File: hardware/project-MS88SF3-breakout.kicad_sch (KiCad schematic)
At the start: 27 parts, among them J1 Conn_02x05_Odd_Even, J2 S2B-PH-SM4-TB(LF)(SN), J3 USB4105-GF-A, J4 Conn_01x12_Pin, J5 Conn_01x16_Pin, U1 MS88SF3_NRF52840

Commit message: Fix ERC error
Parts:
- S1: footprint 435151014824 -> 435151014824:435151014824
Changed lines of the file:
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@@
 			)
 		)
-		(property "Footprint" "435151014824"
+		(property "Footprint" "435151014824:435151014824"
 			(at 82.55 167.64 0)
 			(effects
@@
 			)
 		)
-		(property "Description" ""
+		(property "Description" "435151014824"
 			(at 64.77 167.64 0)
 			(effects

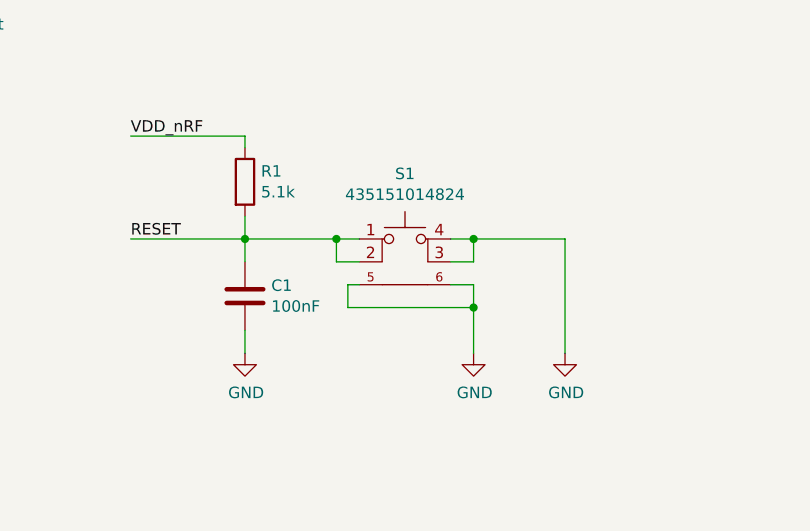
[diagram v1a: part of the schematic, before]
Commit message: Change reset button
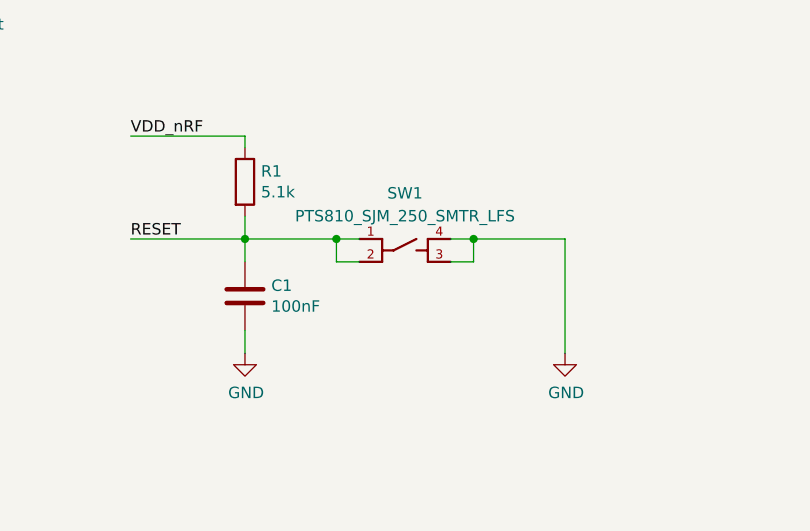
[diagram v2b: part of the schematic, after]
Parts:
- removed S1: 435151014824, 435151014824:435151014824, symbol 435151014824:435151014824
- added SW1: PTS810_SJM_250_SMTR_LFS, PTS810-SJM-250-SMTR-LFS:SW_PTS810_SJM_250_SMTR_LFS, symbol PTS810_SJM_250_SMTR_LFS:PTS810_SJM_250_SMTR_LFS
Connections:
- net GND: now also SW1.3, SW1.4
- net RESET: now also SW1.1, SW1.2
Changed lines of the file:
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@@
 	)
 	(junction
-		(at 72.39 175.26)
-		(diameter 0)
-		(color 0 0 0 0)
-	)
-	(junction
 		(at 229.87 34.29)
 		(diameter 0)
@@
 	(wire
 		(pts
-			(xy 72.39 175.26) (xy 72.39 180.34)
-		)
-		(stroke
-			(width 0)
-			(type default)
-		)
-	)
-	(wire
-		(pts
 			(xy 46.99 165.1) (xy 46.99 167.64)
 		)
@@
 	(wire
 		(pts
-			(xy 72.39 172.72) (xy 72.39 175.26)
-		)
-		(stroke
-			(width 0)
-			(type default)
-		)
-	)
-	(wire
-		(pts
 			(xy 128.27 52.07) (xy 137.16 52.07)
 		)
@@
 	(wire
 		(pts
-			(xy 59.69 172.72) (xy 58.42 172.72)
-		)
-		(stroke
-			(width 0)
-			(type default)
-		)
-	)
-	(wire
-		(pts
 			(xy 100.33 116.84) (xy 91.44 116.84)
 		)
@@
 	(wire
 		(pts
-			(xy 58.42 172.72) (xy 58.42 175.26)
-		)
-		(stroke
-			(width 0)
-			(type default)
-		)
-	)
-	(wire
-		(pts
 			(xy 251.46 125.73) (xy 254 125.73)
 		)
@@
 	(wire
 		(pts
-			(xy 69.85 172.72) (xy 72.39 172.72)
-		)
-		(stroke
-			(width 0)
-			(type default)
-		)
-	)
-	(wire
-		(pts
 			(xy 21.59 63.5) (xy 30.48 63.5)
 		)
@@
 	(wire
 		(pts
-			(xy 58.42 175.26) (xy 72.39 175.26)
-		)
-		(stroke
-			(width 0)
-			(type default)
-		)
-	)
-	(wire
-		(pts
 			(xy 213.36 39.37) (xy 217.17 39.37)
 		)
@@
 	)
 	(symbol
-		(lib_id "435151014824:435151014824")
-		(at 64.77 167.64 0)
-		(unit 1)
-		(exclude_from_sim no)
-		(in_bom yes)
-		(on_board yes)
-		(dnp no)
-		(property "Reference" "S1"
-			(at 64.77 160.401 0)
-			(effects
-				(font
-					(size 1.27 1.27)
-				)
-			)
-		)
-		(property "Value" "435151014824"
-			(at 64.77 162.7124 0)
-			(effects
-				(font
-					(size 1.27 1.27)
-				)
-			)
-		)
-		(property "Footprint" "435151014824:435151014824"
-			(at 82.55 167.64 0)
-			(effects
-				(font
-					(size 1.27 1.27)
-				)
-				(justify left bottom)
-				(hide yes)
-			)
-		)
-		(property "Datasheet" ""
-			(at 64.77 165.1 0)
-			(effects
-				(font
-					(size 1.27 1.27)
-				)
-				(justify left bottom)
-				(hide yes)
-			)
-		)
-		(property "Description" "435151014824"
-			(at 64.77 167.64 0)
-			(effects
-				(font
-					(size 1.27 1.27)
-				)
-				(hide yes)
-			)
-		)
-		(property "PART-NUMBER" "435151014824"
-			(at 82.55 165.1 0)
-			(effects
-				(font
-					(size 1.27 1.27)
-				)
-				(justify left bottom)
-				(hide yes)
-			)
-		)
-		(property "QTY" "9500"
-			(at 74.93 167.64 0)
-			(effects
-				(font
-					(size 1.27 1.27)
-				)
-				(justify left bottom)
-				(hide yes)
-			)
-		)
-		(property "DATASHEET-URL" "https://www.we-online.com/catalog/datasheet/435151014824 .pdf"
-			(at 74.93 170.18 0)
-			(effects
-				(font
-					(size 1.27 1.27)
-				)
-				(justify left bottom)
-				(hide yes)
-			)
-		)
-		(property "H" "1.4mm"
-			(at 74.93 165.1 0)
-			(effects
-				(font
-					(size 1.27 1.27)
-				)
-				(justify left bottom)
-				(hide yes)
-			)
-		)
-		(property "OPERATION-FORCE" "240g"
-			(at 74.93 162.56 0)
-			(effects
-				(font
-					(size 1.27 1.27)
-				)
-				(justify left bottom)
-				(hide yes)
-			)
-		)
-		(property "VALUE" "435151014824"
-			(at 82.55 162.56 0)
-			(effects
-				(font
-					(size 1.27 1.27)
-				)
-				(justify left bottom)
-				(hide yes)
-			)
-		)
-		(pin "5"
-		)
-		(pin "1"
-		)
-		(pin "4"
-		)
-		(pin "3"
-		)
-		(pin "6"
-		)
-		(pin "2"
-		)
-		(instances
-			(project "project-MS88SF3-breakout"
-				(path "/3e0804a6-abc2-4b5d-ae97-2c771c876220"
-					(reference "S1")
-					(unit 1)
-				)
-			)
-		)
-	)
-	(symbol
-		(lib_id "power:GND")
-		(at 72.39 180.34 0)
-		(unit 1)
-		(exclude_from_sim no)
-		(in_bom yes)
-		(on_board yes)
-		(dnp no)
-		(property "Reference" "#PWR03"
-			(at 72.39 186.69 0)
-			(effects
-				(font
-					(size 1.27 1.27)
-				)
-				(hide yes)
-			)
-		)
-		(property "Value" "GND"
-			(at 72.517 184.7342 0)
-			(effects
-				(font
-					(size 1.27 1.27)
-				)
-			)
-		)
-		(property "Footprint" ""
-			(at 72.39 180.34 0)
-			(effects
-				(font
-					(size 1.27 1.27)
-				)
-				(hide yes)
-			)
-		)
-		(property "Datasheet" ""
-			(at 72.39 180.34 0)
-			(effects
-				(font
-					(size 1.27 1.27)
-				)
-				(hide yes)
-			)
-		)
-		(property "Description" ""
-			(at 72.39 180.34 0)
-			(effects
-				(font
-					(size 1.27 1.27)
-				)
-				(hide yes)
-			)
-		)
-		(pin "1"
-		)
-		(instances
-			(project "project-MS88SF3-breakout"
-				(path "/3e0804a6-abc2-4b5d-ae97-2c771c876220"
-					(reference "#PWR03")
-					(unit 1)
-				)
-			)
-		)
-	)
-	(symbol
 		(lib_id "MS88SF3_NRF52840:MS88SF3_NRF52840")
 		(at 60.96 76.2 0)
@@
 					(unit 1)
 				)
+			)
+		)
+	)
+	(symbol
+		(lib_id "PTS810_SJM_250_SMTR_LFS:PTS810_SJM_250_SMTR_LFS")
+		(at 64.77 167.64 0)
+		(unit 1)
+		(exclude_from_sim no)
+		(in_bom yes)
+		(on_board yes)
+		(dnp no)
+		(fields_autoplaced yes)
+		(property "Reference" "SW1"
+			(at 64.77 162.56 0)
+			(effects
+				(font
+					(size 1.27 1.27)
+				)
+			)
+		)
+		(property "Value" "PTS810_SJM_250_SMTR_LFS"
+			(at 64.77 165.1 0)
+			(effects
+				(font
+					(size 1.27 1.27)
+				)
+			)
+		)
+		(property "Footprint" "PTS810-SJM-250-SMTR-LFS:SW_PTS810_SJM_250_SMTR_LFS"
+			(at 64.77 167.64 0)
+			(effects
+				(font
+					(size 1.27 1.27)
+				)
+				(justify bottom)
+				(hide yes)
+			)
+		)
+		(property "Datasheet" ""
+			(at 64.77 167.64 0)
+			(effects
+				(font
+					(size 1.27 1.27)
+				)
+				(hide yes)
+			)
+		)
+		(property "Description" ""
+			(at 64.77 167.64 0)
+			(effects
+				(font
+					(size 1.27 1.27)
+				)
+				(hide yes)
+			)
+		)
+		(property "DigiKey_Part_Number" "CKN10502TR-ND"
+			(at 64.77 167.64 0)
+			(effects
+				(font
+					(size 1.27 1.27)
+				)
+				(justify bottom)
+				(hide yes)
+			)
+		)
+		(property "SnapEDA_Link" "https://www.snapeda.com/parts/PTS810%20SJM%20250%20SMTR%20LFS/C%2526K/view-part/?ref=snap"
+			(at 64.77 167.64 0)
+			(effects
+				(font
+					(size 1.27 1.27)
+				)
+				(justify bottom)
+				(hide yes)
+			)
+		)
+		(property "Description_1" "\nTactile Switch SPST-NO Top Actuated Surface Mount\n"
+			(at 64.77 167.64 0)
+			(effects
+				(font
+					(size 1.27 1.27)
+				)
+				(justify bottom)
+				(hide yes)
+			)
+		)
+		(property "Package" "None"
+			(at 64.77 167.64 0)
+			(effects
+				(font
+					(size 1.27 1.27)
+				)
+				(justify bottom)
+				(hide yes)
+			)
+		)
+		(property "Check_prices" "https://www.snapeda.com/parts/PTS810%20SJM%20250%20SMTR%20LFS/C%2526K/view-part/?ref=eda"
+			(at 64.77 167.64 0)
+			(effects
+				(font
+					(size 1.27 1.27)
+				)
+				(justify bottom)
+				(hide yes)
+			)
+		)
+		(property "STANDARD" "Manufacturer Recommendations"
+			(at 64.77 167.64 0)
+			(effects
+				(font
+					(size 1.27 1.27)
+				)
+				(justify bottom)
+				(hide yes)
+			)
+		)
+		(property "MF" "C&K"
+			(at 64.77 167.64 0)
+			(effects
+				(font
+					(size 1.27 1.27)
+				)
+				(justify bottom)
+				(hide yes)
+			)
+		)
+		(property "MP" "PTS810 SJM 250 SMTR LFS"
+			(at 64.77 167.64 0)
+			(effects
+				(font
+					(size 1.27 1.27)
+				)
+				(justify bottom)
+				(hide yes)
+			)
+		)
+		(property "MANUFACTURER" "CnK"
+			(at 64.77 167.64 0)
+			(effects
+				(font
+					(size 1.27 1.27)
+				)
+				(justify bottom)
+				(hide yes)
+			)
+		)
+		(pin "4"
+		)
+		(pin "3"
+		)
+		(pin "2"
+		)
+		(pin "1"
+		)
+		(instances
+			(project "project-MS88SF3-breakout"
+				(path "/3e0804a6-abc2-4b5d-ae97-2c771c876220"
+					(reference "SW1")
+					(unit 1)
+				)

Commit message: User SolderJumper-2 footprint without center soldermask
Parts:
- JP1: footprint Jumper:SolderJumper-2_P1.3mm_Bridged_RoundedPad1.0x1.5mm -> mine:SolderJumper-2_P1.3mm_Bridged_RoundedPad1.0x1.5mm
- JP2: footprint Jumper:SolderJumper-2_P1.3mm_Open_RoundedPad1.0x1.5mm -> mine:SolderJumper-2_P1.3mm_Open_RoundedPad1.0x1.5mm
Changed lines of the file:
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@@
 			)
 		)
-		(property "Footprint" "Jumper:SolderJumper-2_P1.3mm_Bridged_RoundedPad1.0x1.5mm"
+		(property "Footprint" "mine:SolderJumper-2_P1.3mm_Bridged_RoundedPad1.0x1.5mm"
 			(at 236.22 39.37 0)
 			(effects
@@
 			)
 		)
-		(property "Footprint" "Jumper:SolderJumper-2_P1.3mm_Open_RoundedPad1.0x1.5mm"
+		(property "Footprint" "mine:SolderJumper-2_P1.3mm_Open_RoundedPad1.0x1.5mm"
 			(at 242.57 30.48 0)
 			(effects

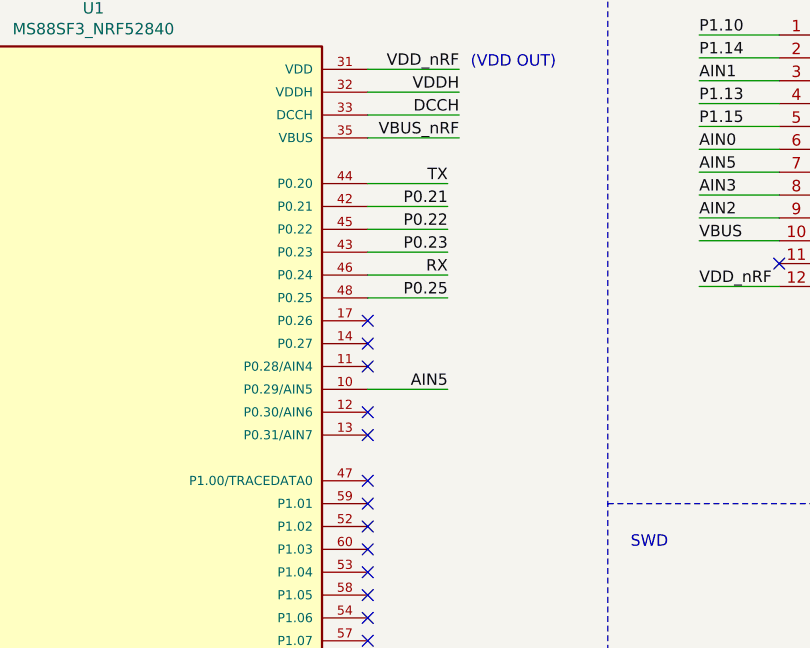
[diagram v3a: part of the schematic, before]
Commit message: Move TX to SWO
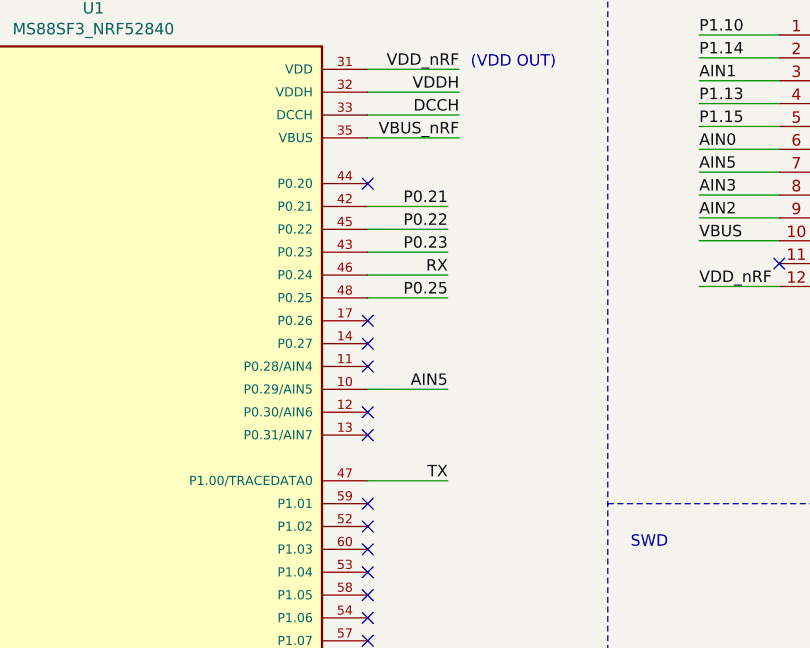
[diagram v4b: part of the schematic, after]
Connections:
- net TX: now also U1.47 (P1.00/TRACEDATA0); no longer U1.44 (P0.20)
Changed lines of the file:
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@@
 	)
 	(no_connect
-		(at 91.44 78.74)
+		(at 91.44 45.72)
 	)
 	(no_connect
@@
 	(wire
 		(pts
-			(xy 100.33 45.72) (xy 91.44 45.72)
+			(xy 100.33 78.74) (xy 91.44 78.74)
 		)
 		(stroke
@@
 	)
 	(label "TX"
-		(at 100.33 45.72 180)
-		(fields_autoplaced yes)
-		(effects
+		(at 100.33 78.74 180)
+		(fields_autoplaced yes)
+		(effects

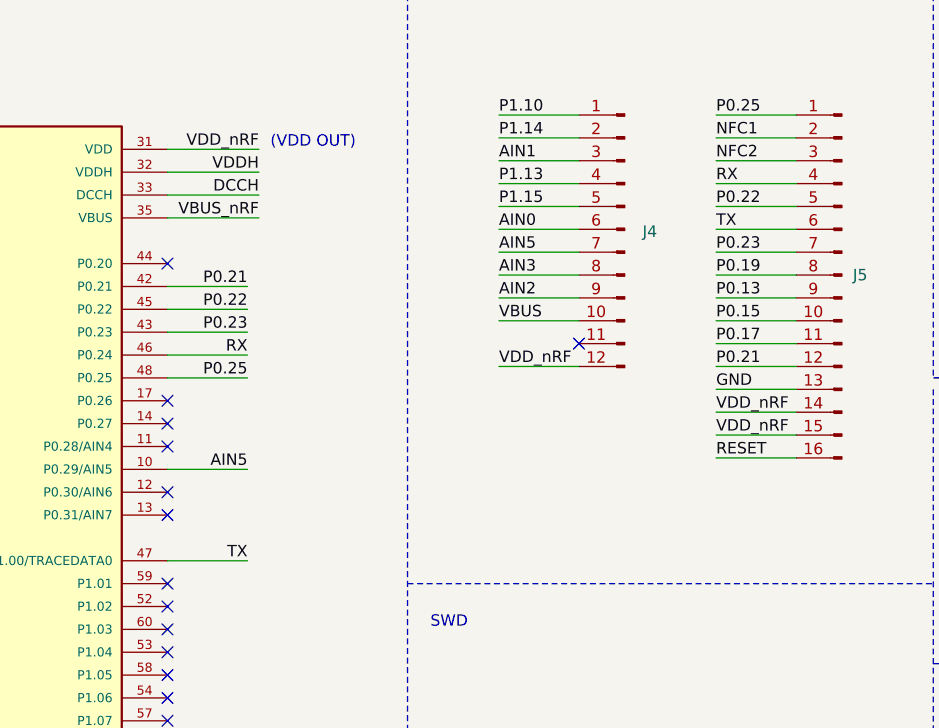
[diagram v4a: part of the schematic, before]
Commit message: Change header RX/TX to gpios
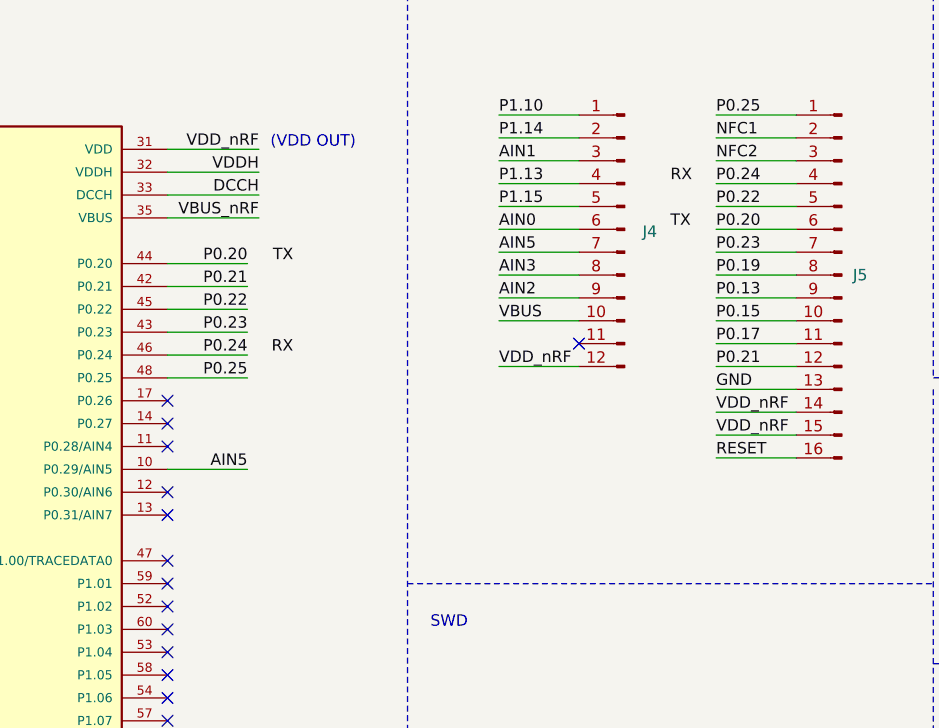
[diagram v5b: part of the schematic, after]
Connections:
- net RX: no longer J5.4 (Pin_4), U1.46 (P0.24)
- net TX: no longer J5.6 (Pin_6), U1.47 (P1.00/TRACEDATA0)
- net P0.20: now reaches U1.44 (P0.20)
- net P0.20: now also J5.6 (Pin_6)
- new net P0.24: J5.4 (Pin_4), U1.46 (P0.24)
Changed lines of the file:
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@@
 	)
 	(no_connect
-		(at 91.44 45.72)
+		(at 91.44 78.74)
 	)
 	(no_connect
@@
 	(wire
 		(pts
-			(xy 100.33 78.74) (xy 91.44 78.74)
+			(xy 100.33 45.72) (xy 91.44 45.72)
 		)
 		(stroke
@@
 		)
 	)
+	(label "P0.24"
+		(at 152.4 36.83 0)
+		(fields_autoplaced yes)
+		(effects
+			(font
+				(size 1.27 1.27)
+			)
+			(justify left bottom)
+		)
+	)
+	(label "P0.24"
+		(at 100.33 55.88 180)
+		(fields_autoplaced yes)
+		(effects
+			(font
+				(size 1.27 1.27)
+			)
+			(justify right bottom)
+		)
+	)
 	(label "P0.21"
 		(at 152.4 57.15 0)
@@
 	)
 	(label "TX"
-		(at 152.4 41.91 0)
+		(at 147.32 41.91 0)
 		(fields_autoplaced yes)
 		(effects
@@
 	)
 	(label "TX"
-		(at 100.33 78.74 180)
+		(at 105.41 45.72 180)
 		(fields_autoplaced yes)
 		(effects
@@
 	)
 	(label "RX"
-		(at 100.33 55.88 180)
+		(at 105.41 55.88 180)
 		(fields_autoplaced yes)
 		(effects
@@
 	)
 	(label "RX"
-		(at 152.4 36.83 0)
+		(at 147.32 36.83 0)
 		(fields_autoplaced yes)
 		(effects
@@
 		)
 	)
+	(label "P0.20"
+		(at 100.33 45.72 180)
+		(fields_autoplaced yes)
+		(effects
+			(font
+				(size 1.27 1.27)
+			)
+			(justify right bottom)
+		)
+	)
 	(label "D+"
 		(at 186.69 146.05 0)
@@
 		)
 	)
+	(label "P0.20"
+		(at 152.4 41.91 0)
+		(fields_autoplaced yes)
+		(effects
+			(font
+				(size 1.27 1.27)
+			)
+			(justify left bottom)
+		)
+	)
